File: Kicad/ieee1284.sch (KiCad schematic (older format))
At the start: 4 parts, among them J13 DB25_Female_MountingHoles, U12 74LS138, U13 74LS245, U14 74LS573

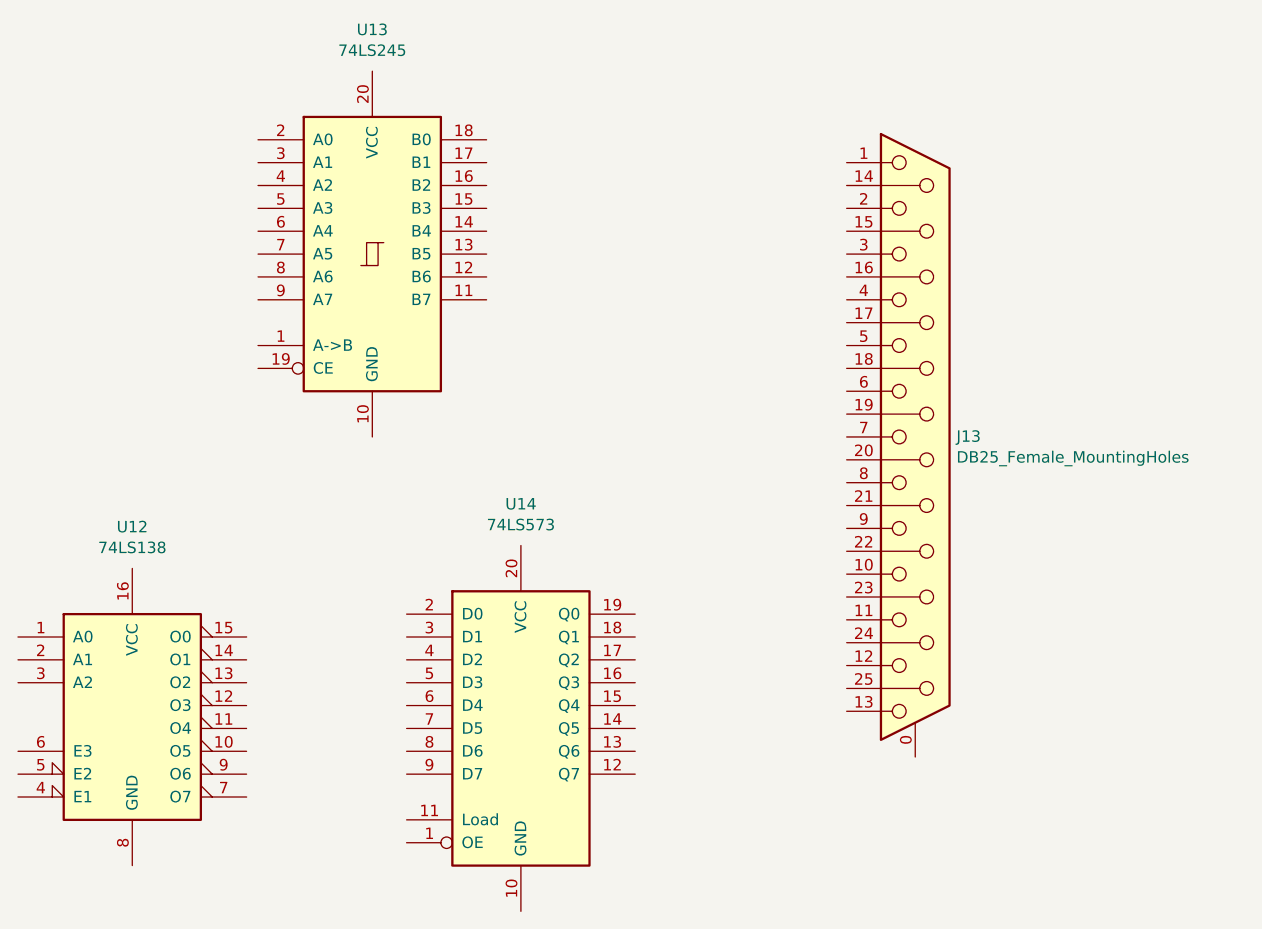
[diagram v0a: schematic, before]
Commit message: Removed USB FS hub. Added stacked USB A connector.
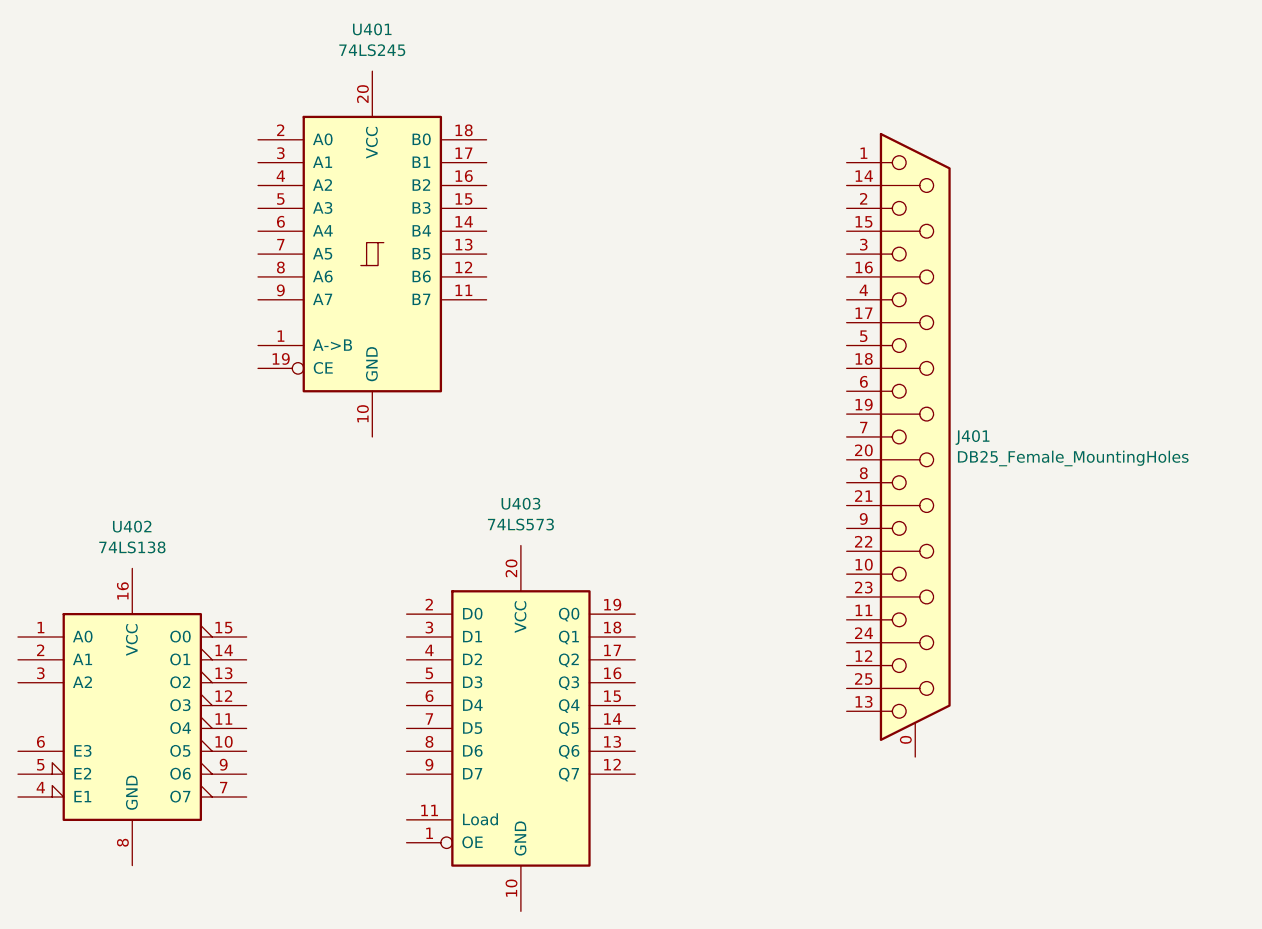
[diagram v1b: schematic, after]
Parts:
- renumbered J13 to J401, U13 to U401, U12 to U402, U14 to U403
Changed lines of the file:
@@
 $Descr A4 11693 8268
 encoding utf-8
-Sheet 4 7
+Sheet 4 6
 Title "Neotron F7"
 Date "2020-05-25"
@@
 P 5950 4300
 AR Path="/5EF27DDC" Ref="U?"  Part="1"
-AR Path="/5EF25502/5EF27DDC" Ref="U14"  Part="1"
-F 0 "U14" H 5950 5281 50  0000 C CNN
+AR Path="/5EF25502/5EF27DDC" Ref="U403"  Part="1"
+F 0 "U403" H 5950 5281 50  0000 C CNN
 F 1 "74LS573" H 5950 5190 50  0000 C CNN
 F 2 "" H 5950 4300 50  0001 C CNN
@@
 P 5300 2225
 AR Path="/5EF27DE2" Ref="U?"  Part="1"
-AR Path="/5EF25502/5EF27DE2" Ref="U13"  Part="1"
-F 0 "U13" H 5300 3206 50  0000 C CNN
+AR Path="/5EF25502/5EF27DE2" Ref="U401"  Part="1"
+F 0 "U401" H 5300 3206 50  0000 C CNN
 F 1 "74LS245" H 5300 3115 50  0000 C CNN
 F 2 "" H 5300 2225 50  0001 C CNN
@@
 P 4250 4200
 AR Path="/5EF27DE8" Ref="U?"  Part="1"
-AR Path="/5EF25502/5EF27DE8" Ref="U12"  Part="1"
-F 0 "U12" H 4250 4981 50  0000 C CNN
+AR Path="/5EF25502/5EF27DE8" Ref="U402"  Part="1"
+F 0 "U402" H 4250 4981 50  0000 C CNN
 F 1 "74LS138" H 4250 4890 50  0000 C CNN
 F 2 "Package_SO:SOIC-16_3.9x9.9mm_P1.27mm" H 4250 4200 50  0001 C CNN
@@
 $EndComp
 $Comp
-L Connector:DB25_Female_MountingHoles J13
+L Connector:DB25_Female_MountingHoles J401
 U 1 1 5EF280B8
 P 7675 3025
-F 0 "J13" H 7855 3027 50  0000 L CNN
+F 0 "J401" H 7855 3027 50  0000 L CNN
 F 1 "DB25_Female_MountingHoles" H 7855 2936 50  0000 L CNN
 F 2 "" H 7675 3025 50  0001 C CNN
